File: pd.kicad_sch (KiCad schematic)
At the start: 1 part

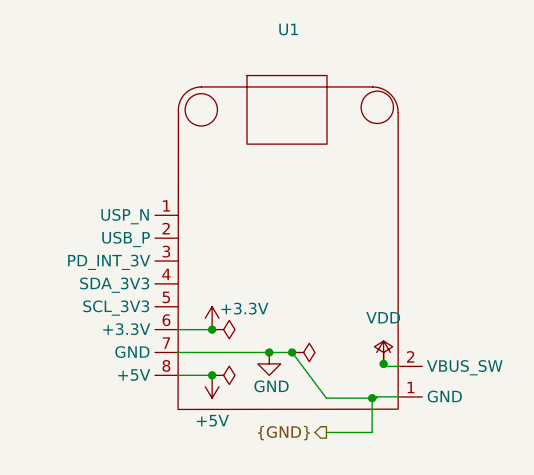
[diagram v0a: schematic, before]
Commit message: updated architecture page
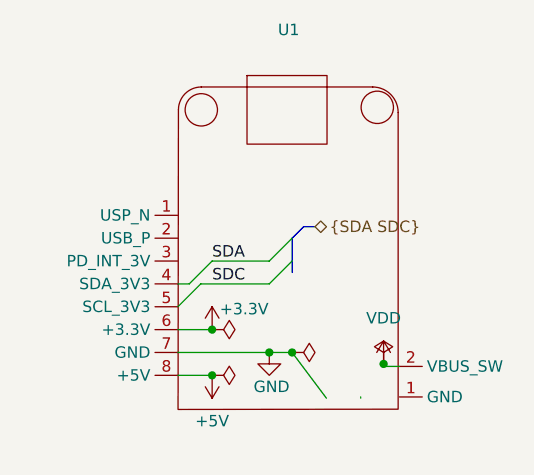
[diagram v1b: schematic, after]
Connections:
- net GND: no longer U1.1 (GND)
- net SDA: now reaches U1.4 (SDA_3V3)
- net SDC: now reaches U1.5 (SCL_3V3)
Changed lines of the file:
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@@
 		(color 0 0 0 0)
 	)
-	(junction
-		(at 163.83 110.49)
-		(diameter 0)
-		(color 0 0 0 0)
-	)
-	(wire
-		(pts
-			(xy 163.83 114.3) (xy 163.83 110.49)
-		)
+	(bus_entry
+		(at 154.94 92.71)
+		(size -2.54 2.54)
 		(stroke
 			(width 0)
@@
 		)
 	)
-	(wire
-		(pts
-			(xy 158.75 110.49) (xy 163.83 110.49)
-		)
+	(bus_entry
+		(at 154.94 95.25)
+		(size -2.54 2.54)
 		(stroke
 			(width 0)
@@
 		(pts
 			(xy 146.05 107.95) (xy 142.24 107.95)
-		)
-		(stroke
-			(width 0)
-			(type default)
-		)
-	)
-	(wire
-		(pts
-			(xy 163.83 114.3) (xy 158.75 114.3)
 		)
 		(stroke
@@
 	(wire
 		(pts
-			(xy 164.3188 110.3527) (xy 166.8588 110.3527)
+			(xy 144.78 97.79) (xy 152.4 97.79)
+		)
+		(stroke
+			(width 0)
+			(type default)
+		)
+	)
+	(wire
+		(pts
+			(xy 143.51 97.79) (xy 146.05 95.25)
+		)
+		(stroke
+			(width 0)
+			(type default)
+		)
+	)
+	(bus
+		(pts
+			(xy 154.94 92.71) (xy 156.21 91.44)
+		)
+		(stroke
+			(width 0)
+			(type default)
+		)
+	)
+	(wire
+		(pts
+			(xy 142.24 100.33) (xy 144.78 97.79)
+		)
+		(stroke
+			(width 0)
+			(type default)
+		)
+	)
+	(bus
+		(pts
+			(xy 154.94 95.25) (xy 154.94 92.71)
+		)
+		(stroke
+			(width 0)
+			(type default)
+		)
+	)
+	(wire
+		(pts
+			(xy 142.24 97.79) (xy 143.51 97.79)
 		)
 		(stroke
@@
 	(wire
 		(pts
-			(xy 164.3188 110.49) (xy 163.83 110.49)
+			(xy 165.1 106.9588) (xy 165.1 106.68)
+		)
+		(stroke
+			(width 0)
+			(type default)
+		)
+	)
+	(bus
+		(pts
+			(xy 154.94 96.52) (xy 154.94 95.25)
 		)
 		(stroke
@@
 	(wire
 		(pts
-			(xy 165.1 106.9588) (xy 165.1 106.68)
-		)
-		(stroke
-			(width 0)
-			(type default)
-		)
-	)
-	(wire
-		(pts
-			(xy 164.3188 110.3527) (xy 164.3188 110.49)
+			(xy 162.56 110.3527) (xy 162.56 110.49)
 		)
 		(stroke
@@
 		)
 	)
-	(hierarchical_label "{GND}"
-		(shape output)
-		(at 158.75 114.3 180)
+	(wire
+		(pts
+			(xy 146.05 95.25) (xy 152.4 95.25)
+		)
+		(stroke
+			(width 0)
+			(type default)
+		)
+	)
+	(bus
+		(pts
+			(xy 156.21 91.44) (xy 157.48 91.44)
+		)
+		(stroke
+			(width 0)
+			(type default)
+		)
+	)
+	(label "SDC"
+		(at 146.05 97.79 0)
 		(effects
 			(font
 				(size 1.27 1.27)
 			)
-			(justify right)
+			(justify left bottom)
 		)
 	)
+	(label "SDA"
+		(at 146.05 95.25 0)
+		(effects
+			(font
+				(size 1.27 1.27)
+			)
+			(justify left bottom)
+		)
+	)
+	(hierarchical_label "{SDA SDC}"
+		(shape bidirectional)
+		(at 157.48 91.44 0)
+		(effects
+			(font
+				(size 1.27 1.27)
+			)
+			(justify left)
+		)
+	)

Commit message: begin pcb
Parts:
- U1: footprint (none) -> Audio_Module:rotopd
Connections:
- net GND: now also U1.1 (GND)
- net SDA: now also U1.5 (SCL_3V3); no longer U1.4 (SDA_3V3)
- net SDC: no longer U1.5 (SCL_3V3)
- no-connect marks 0 -> 3
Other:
- moved on the sheet: U1
